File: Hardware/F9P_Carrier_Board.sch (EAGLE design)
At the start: 82 parts, among them J4 U.FL, J5 QWIIC_RIGHT_ANGLE, J6 MICROMOD-2222-C, J8 JTAG, U1 U-BLOX_ZED-F9P, U5 AP7361C-33

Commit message: Updates nets on the 100k at VREG, adds descpription of SPI jumper, adds VBAT testpoint
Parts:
- added TP3: TEST-POINT3X5, SparkFun-Connectors:TEST-POINT3X5
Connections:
- net V_BATT: now also TP3.1
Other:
- note added: "Close this jumper to enable SPI."
- moved on the sheet: BYP, C1, C13, C2, C5, C6, C7, D1, F2, MEAS, R5, U5

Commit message: Renames the erroneously named SCL/CLK net to SCLK/SCK
* Reroutes so that SCL and SCK are connected
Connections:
- removed net SCL/CLK: J10.7, J5.4, J6.SPI_SCK, R12A.2
- net SCL/SCK: now also J10.7, J5.4, J6.SPI_SCK, R12A.2
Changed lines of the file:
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@@
 <pinref part="J6" gate="J1" pin="I2C_SCL"/>
+</segment>
+<segment>
+<wire x1="106.68" y1="193.04" x2="109.22" y2="193.04" width="0.1524" layer="91"/>
+<label x="109.22" y="193.04" size="1.27" layer="95" xref="yes"/>
+<pinref part="J6" gate="J1" pin="SPI_SCK"/>
+</segment>
+<segment>
+<pinref part="J5" gate="G$1" pin="4"/>
+<wire x1="276.86" y1="63.5" x2="271.78" y2="63.5" width="0.1524" layer="91"/>
+<label x="276.86" y="63.5" size="1.27" layer="95" xref="yes"/>
+</segment>
+<segment>
+<wire x1="302.26" y1="50.8" x2="314.96" y2="50.8" width="0.1524" layer="91"/>
+<label x="314.96" y="50.8" size="1.27" layer="95" font="vector" xref="yes"/>
+<pinref part="J10" gate="G$1" pin="7"/>
+</segment>
+<segment>
+<wire x1="365.76" y1="170.18" x2="368.3" y2="170.18" width="0.1524" layer="91"/>
+<label x="368.3" y="170.18" size="1.27" layer="95" xref="yes"/>
+<pinref part="R12" gate="A" pin="2"/>
 </segment>
 </net>
@@
 </segment>
 </net>
-<net name="SCL/CLK" class="0">
-<segment>
-<pinref part="J5" gate="G$1" pin="4"/>
-<wire x1="276.86" y1="63.5" x2="271.78" y2="63.5" width="0.1524" layer="91"/>
-<label x="276.86" y="63.5" size="1.27" layer="95" xref="yes"/>
-</segment>
-<segment>
-<wire x1="106.68" y1="193.04" x2="109.22" y2="193.04" width="0.1524" layer="91"/>
-<label x="109.22" y="193.04" size="1.27" layer="95" xref="yes"/>
-<pinref part="J6" gate="J1" pin="SPI_SCK"/>
-</segment>
-<segment>
-<wire x1="302.26" y1="50.8" x2="314.96" y2="50.8" width="0.1524" layer="91"/>
-<label x="314.96" y="50.8" size="1.27" layer="95" font="vector" xref="yes"/>
-<pinref part="J10" gate="G$1" pin="7"/>
-</segment>
-<segment>
-<wire x1="365.76" y1="170.18" x2="368.3" y2="170.18" width="0.1524" layer="91"/>
-<label x="368.3" y="170.18" size="1.27" layer="95" xref="yes"/>
-<pinref part="R12" gate="A" pin="2"/>
-</segment>
-</net>

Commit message: Rolls version to v10, moves some vias, deletes I2C_INT net (not used)
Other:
- note added: "v10"
- note removed: "v01"
- moved on the sheet: C8, E1, FB1, J4, J9, R17

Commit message: Adjusts battery placement on board so that it's mostly out of the way
* Breaks out a few general purpose pins to a 6 pin header at the bottom of the board
* Adds text to led and enable jumpers
* Adds text about interrupt
* Adds connection from interrupt on ublox module to micromod connector.
* Fixes "processor" silk
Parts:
- added J7: (no value), SparkFun-Connectors:CONN_06NO_SILK_NO_POP
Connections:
- removed net I2C_!INT: J6.I2C_!INT!
- new net A0: J6.A0, J7.2
- new net A1: J6.A1, J7.3
- new net D1: J6.D1/CAM_TRIG, J7.4
- new net G0/D2: J6.G0/BUS0, J7.5
- net GND: now also J7.1, J7.6
- net INT: now also J6.I2C_!INT!
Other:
- note added: "Close "EN" jumper to allow processor control over 3.3V power."
- note added: "Cut jumpers to remove respective LEDs"
- note added: "Interrupt is not enabled by default. Check ublox datasheet for more information."
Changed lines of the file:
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@@
 <part name="TP3" library="SparkFun-Connectors" deviceset="TEST-POINT" device="3X5"/>
 <part name="SUPPLY15" library="SparkFun-PowerSymbols" deviceset="V_BATT" device=""/>
+<part name="J7" library="SparkFun-Connectors" deviceset="CONN_06" device="NO_SILK_NO_POP"/>
+<part name="GND26" library="SparkFun-PowerSymbols" deviceset="GND" device=""/>
 </parts>
 <sheets>
@@
 <text x="388.62" y="165.1" size="1.778" layer="97" font="vector">Close this jumper
 to enable SPI.</text>
+<text x="53.34" y="60.96" size="1.778" layer="97" font="vector">Cut jumpers to remove respective LEDs</text>
+<text x="5.08" y="208.28" size="1.778" layer="97" font="vector">Close "EN" jumper to allow processor
+control over 3.3V power.</text>
+<text x="370.84" y="187.96" size="1.778" layer="97" font="vector">Interrupt is not enabled by default.
+Check ublox datasheet for more information.</text>
+<wire x1="393.7" y1="185.42" x2="393.7" y2="175.26" width="0.1524" layer="97" style="dashdot"/>
+<wire x1="393.7" y1="175.26" x2="375.92" y2="175.26" width="0.1524" layer="97" style="dashdot"/>
 </plain>
 <instances>
@@
 <instance part="SUPPLY15" gate="G$1" x="195.58" y="10.16" smashed="yes">
 <attribute name="VALUE" x="195.58" y="12.954" size="1.778" layer="96" align="bottom-center"/>
+</instance>
+<instance part="J7" gate="G$1" x="264.16" y="17.78" smashed="yes">
+<attribute name="VALUE" x="259.08" y="7.874" size="1.778" layer="96" font="vector"/>
+<attribute name="NAME" x="259.08" y="28.448" size="1.778" layer="95" font="vector"/>
+</instance>
+<instance part="GND26" gate="1" x="271.78" y="7.62" smashed="yes">
+<attribute name="VALUE" x="271.78" y="7.366" size="1.778" layer="96" align="top-center"/>
 </instance>
 </instances>
@@
 <pinref part="GND7" gate="1" pin="GND"/>
 <wire x1="210.82" y1="195.58" x2="210.82" y2="185.42" width="0.1524" layer="91"/>
+</segment>
+<segment>
+<pinref part="J7" gate="G$1" pin="6"/>
+<wire x1="269.24" y1="25.4" x2="271.78" y2="25.4" width="0.1524" layer="91"/>
+<wire x1="271.78" y1="25.4" x2="271.78" y2="12.7" width="0.1524" layer="91"/>
+<pinref part="J7" gate="G$1" pin="1"/>
+<wire x1="271.78" y1="12.7" x2="271.78" y2="10.16" width="0.1524" layer="91"/>
+<wire x1="269.24" y1="12.7" x2="271.78" y2="12.7" width="0.1524" layer="91"/>
+<junction x="271.78" y="12.7"/>
+<pinref part="GND26" gate="1" pin="GND"/>
 </segment>
 </net>
@@
 </segment>
 </net>
-<net name="I2C_!INT" class="0">
-<segment>
-<wire x1="60.96" y1="139.7" x2="58.42" y2="139.7" width="0.1524" layer="91"/>
-<pinref part="J6" gate="J1" pin="I2C_!INT!"/>
-</segment>
-</net>
 <net name="N$5" class="0">
 <segment>
@@
 <label x="368.3" y="175.26" size="1.27" layer="95" xref="yes"/>
 <pinref part="R11" gate="A" pin="2"/>
+</segment>
+<segment>
+<pinref part="J6" gate="J1" pin="I2C_!INT!"/>
+<wire x1="60.96" y1="139.7" x2="58.42" y2="139.7" width="0.1524" layer="91"/>
+<label x="58.42" y="139.7" size="1.27" layer="95" rot="R180" xref="yes"/>
 </segment>
 </net>
@@
 </segment>
 </net>
+<net name="D1" class="0">
+<segment>
+<pinref part="J6" gate="J1" pin="D1/CAM_TRIG"/>
+<wire x1="106.68" y1="167.64" x2="109.22" y2="167.64" width="0.1524" layer="91"/>
+<label x="109.22" y="167.64" size="1.27" layer="95" xref="yes"/>
+</segment>
+<segment>
+<pinref part="J7" gate="G$1" pin="4"/>
+<wire x1="269.24" y1="20.32" x2="274.32" y2="20.32" width="0.1524" layer="91"/>
+<label x="274.32" y="20.32" size="1.27" layer="95" xref="yes"/>
+</segment>
+</net>
+<net name="G0/D2" class="0">
+<segment>
+<pinref part="J6" gate="J1" pin="G0/BUS0"/>
+<wire x1="106.68" y1="144.78" x2="109.22" y2="144.78" width="0.1524" layer="91"/>
+<label x="109.22" y="144.78" size="1.27" layer="95" xref="yes"/>
+</segment>
+<segment>
+<pinref part="J7" gate="G$1" pin="5"/>
+<wire x1="269.24" y1="22.86" x2="274.32" y2="22.86" width="0.1524" layer="91"/>
+<label x="274.32" y="22.86" size="1.27" layer="95" xref="yes"/>
+</segment>
+</net>
+<net name="A1" class="0">
+<segment>
+<pinref part="J6" gate="J1" pin="A1"/>
+<wire x1="106.68" y1="177.8" x2="109.22" y2="177.8" width="0.1524" layer="91"/>
+<label x="109.22" y="177.8" size="1.27" layer="95" xref="yes"/>
+</segment>
+<segment>
+<pinref part="J7" gate="G$1" pin="3"/>
+<wire x1="269.24" y1="17.78" x2="274.32" y2="17.78" width="0.1524" layer="91"/>
+<label x="274.32" y="17.78" size="1.27" layer="95" xref="yes"/>
+</segment>
+</net>
+<net name="A0" class="0">
+<segment>
+<pinref part="J6" gate="J1" pin="A0"/>
+<wire x1="106.68" y1="180.34" x2="109.22" y2="180.34" width="0.1524" layer="91"/>
+<label x="109.22" y="180.34" size="1.27" layer="95" xref="yes"/>
+</segment>
+<segment>
+<pinref part="J7" gate="G$1" pin="2"/>
+<wire x1="269.24" y1="15.24" x2="274.32" y2="15.24" width="0.1524" layer="91"/>
+<label x="274.32" y="15.24" size="1.27" layer="95" xref="yes"/>
+</segment>
+</net>

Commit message: Adds I2C address to schematic, swaps SMA connector to female version
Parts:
- J4: device SparkFun-RF:ANTENNA-SMA-GROUNDEDEDGE_RPSMA_SMD -> SparkFun-RF:ANTENNA-SMA-GROUNDEDEDGE_SMA_SMD
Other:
- note added: "I2C unshifted 7 bit address: 0x42"
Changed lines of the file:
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@@
 <part name="R16" library="SparkFun-Resistors" deviceset="27OHM" device=""/>
 <part name="D4" library="SparkFun-IC-Power" deviceset="PRTR5V0U2" device="F"/>
-<part name="J4" library="SparkFun-RF" deviceset="ANTENNA-SMA-GROUNDED" device="EDGE_RPSMA_SMD" value="U.FL"/>
+<part name="J4" library="SparkFun-RF" deviceset="ANTENNA-SMA-GROUNDED" device="EDGE_SMA_SMD" value="U.FL"/>
 <part name="GND14" library="SparkFun-PowerSymbols" deviceset="GND" device=""/>
 <part name="GND17" library="SparkFun-PowerSymbols" deviceset="GND" device=""/>
@@
 <wire x1="393.7" y1="185.42" x2="393.7" y2="175.26" width="0.1524" layer="97" style="dashdot"/>
 <wire x1="393.7" y1="175.26" x2="375.92" y2="175.26" width="0.1524" layer="97" style="dashdot"/>
+<text x="312.42" y="116.84" size="1.778" layer="97" font="vector">I2C unshifted 7 bit address: 0x42</text>
 </plain>
 <instances>

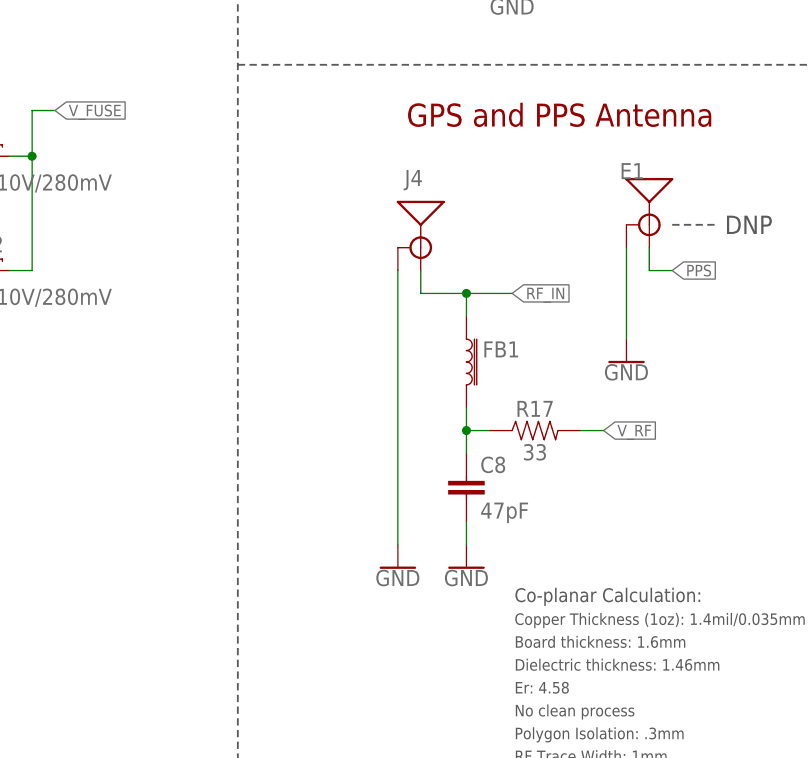
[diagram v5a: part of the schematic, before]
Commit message: Adds diode protection to antenna
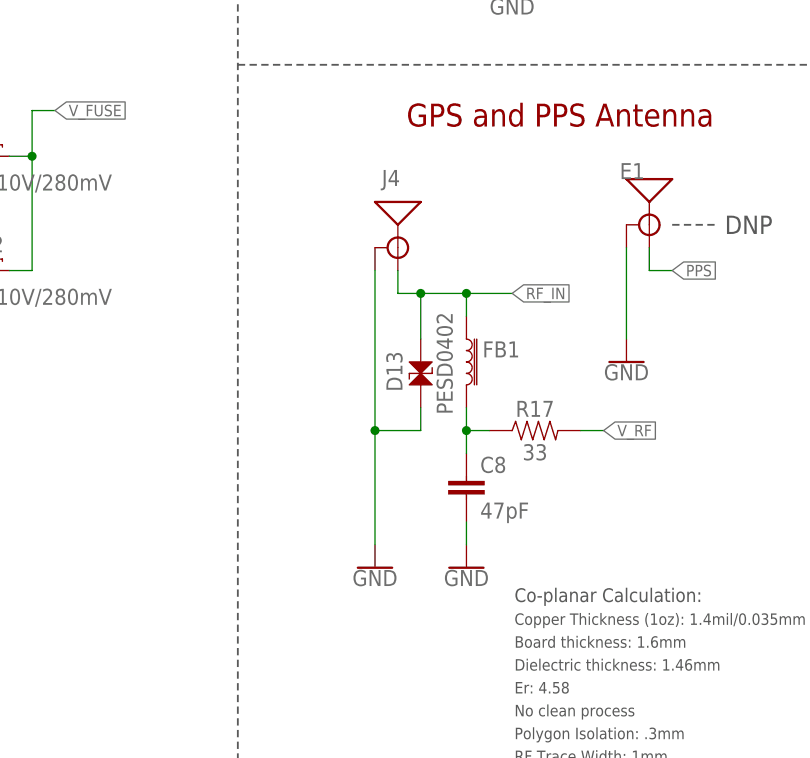
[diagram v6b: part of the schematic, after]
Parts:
- added D13: PESD0402, SparkFun-DiscreteSemi:PESD0402
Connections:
- net GND: now also D13.1
- net RF_IN: now also D13.2
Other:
- moved on the sheet: J4
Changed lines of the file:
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@@
 <layer number="56" name="wert" color="7" fill="1" visible="no" active="no"/>
 <layer number="57" name="tCAD" color="7" fill="1" visible="no" active="no"/>
+<layer number="58" name="bCAD" color="7" fill="1" visible="no" active="no"/>
 <layer number="59" name="tCarbon" color="7" fill="1" visible="no" active="no"/>
 <layer number="60" name="bCarbon" color="7" fill="1" visible="no" active="no"/>
@@
 <layer number="250" name="Descript" color="3" fill="1" visible="no" active="no"/>
 <layer number="251" name="SMDround" color="12" fill="11" visible="no" active="no"/>
+<layer number="253" name="Extra" color="7" fill="1" visible="no" active="no"/>
 <layer number="254" name="cooling" color="7" fill="1" visible="no" active="no"/>
 <layer number="255" name="routoute" color="7" fill="1" visible="no" active="no"/>
@@
 <part name="J7" library="SparkFun-Connectors" deviceset="CONN_06" device="NO_SILK_NO_POP"/>
 <part name="GND26" library="SparkFun-PowerSymbols" deviceset="GND" device=""/>
+<part name="D13" library="SparkFun-DiscreteSemi" deviceset="PESD0402" device=""/>
 </parts>
 <sheets>
@@
 <attribute name="VALUE" x="342.9" y="243.586" size="1.778" layer="96" align="top-left"/>
 </instance>
-<instance part="J4" gate="G$1" x="187.96" y="195.58" smashed="yes" rot="MR0">
-<attribute name="NAME" x="188.214" y="202.438" size="1.778" layer="95" rot="MR0"/>
-</instance>
-<instance part="GND14" gate="1" x="185.42" y="160.02" smashed="yes" rot="MR0">
-<attribute name="VALUE" x="185.42" y="159.766" size="1.778" layer="96" rot="MR0" align="top-center"/>
+<instance part="J4" gate="G$1" x="185.42" y="195.58" smashed="yes" rot="MR0">
+<attribute name="NAME" x="185.674" y="202.438" size="1.778" layer="95" rot="MR0"/>
+</instance>
+<instance part="GND14" gate="1" x="182.88" y="160.02" smashed="yes" rot="MR0">
+<attribute name="VALUE" x="182.88" y="159.766" size="1.778" layer="96" rot="MR0" align="top-center"/>
 </instance>
 <instance part="GND17" gate="1" x="193.04" y="160.02" smashed="yes">
@@
 <instance part="GND26" gate="1" x="271.78" y="7.62" smashed="yes">
 <attribute name="VALUE" x="271.78" y="7.366" size="1.778" layer="96" align="top-center"/>
+</instance>
+<instance part="D13" gate="G$1" x="187.96" y="180.34" smashed="yes" rot="R90">
+<attribute name="NAME" x="185.928" y="179.578" size="1.778" layer="95" font="vector" rot="R90"/>
+<attribute name="VALUE" x="189.738" y="177.038" size="1.778" layer="96" font="vector" rot="R90" align="top-left"/>
 </instance>
 </instances>
@@
 <pinref part="J4" gate="G$1" pin="GND"/>
 <pinref part="GND14" gate="1" pin="GND"/>
-<wire x1="185.42" y1="193.04" x2="185.42" y2="162.56" width="0.1524" layer="91"/>
+<wire x1="182.88" y1="193.04" x2="182.88" y2="175.26" width="0.1524" layer="91"/>
+<pinref part="D13" gate="G$1" pin="1"/>
+<wire x1="182.88" y1="175.26" x2="182.88" y2="162.56" width="0.1524" layer="91"/>
+<wire x1="187.96" y1="177.8" x2="187.96" y2="175.26" width="0.1524" layer="91"/>
+<wire x1="187.96" y1="175.26" x2="182.88" y2="175.26" width="0.1524" layer="91"/>
+<junction x="182.88" y="175.26"/>
 </segment>
 <segment>
@@
 <pinref part="J4" gate="G$1" pin="SIGNAL"/>
 <wire x1="193.04" y1="190.5" x2="187.96" y2="190.5" width="0.1524" layer="91"/>
-<wire x1="187.96" y1="190.5" x2="187.96" y2="193.04" width="0.1524" layer="91"/>
+<wire x1="187.96" y1="190.5" x2="185.42" y2="190.5" width="0.1524" layer="91"/>
+<wire x1="185.42" y1="190.5" x2="185.42" y2="193.04" width="0.1524" layer="91"/>
 <junction x="193.04" y="190.5"/>
 <pinref part="FB1" gate="G$1" pin="1"/>
-</segment>
-<segment>
+<pinref part="D13" gate="G$1" pin="2"/>
+<wire x1="187.96" y1="185.42" x2="187.96" y2="190.5" width="0.1524" layer="91"/>
+<junction x="187.96" y="190.5"/>
+</segment>
+<segment>

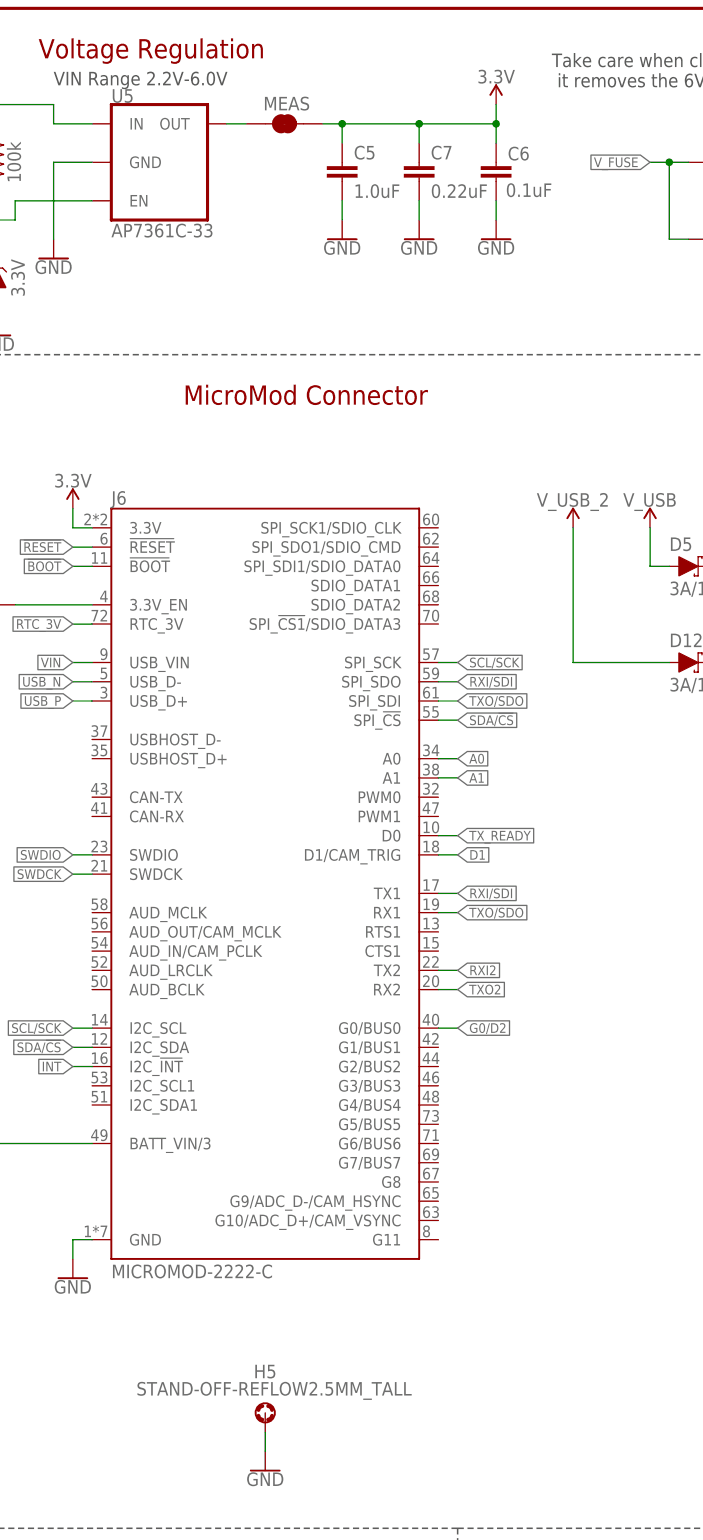
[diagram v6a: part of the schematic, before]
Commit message: Updates silk, moves 1x6 header to the left .005"
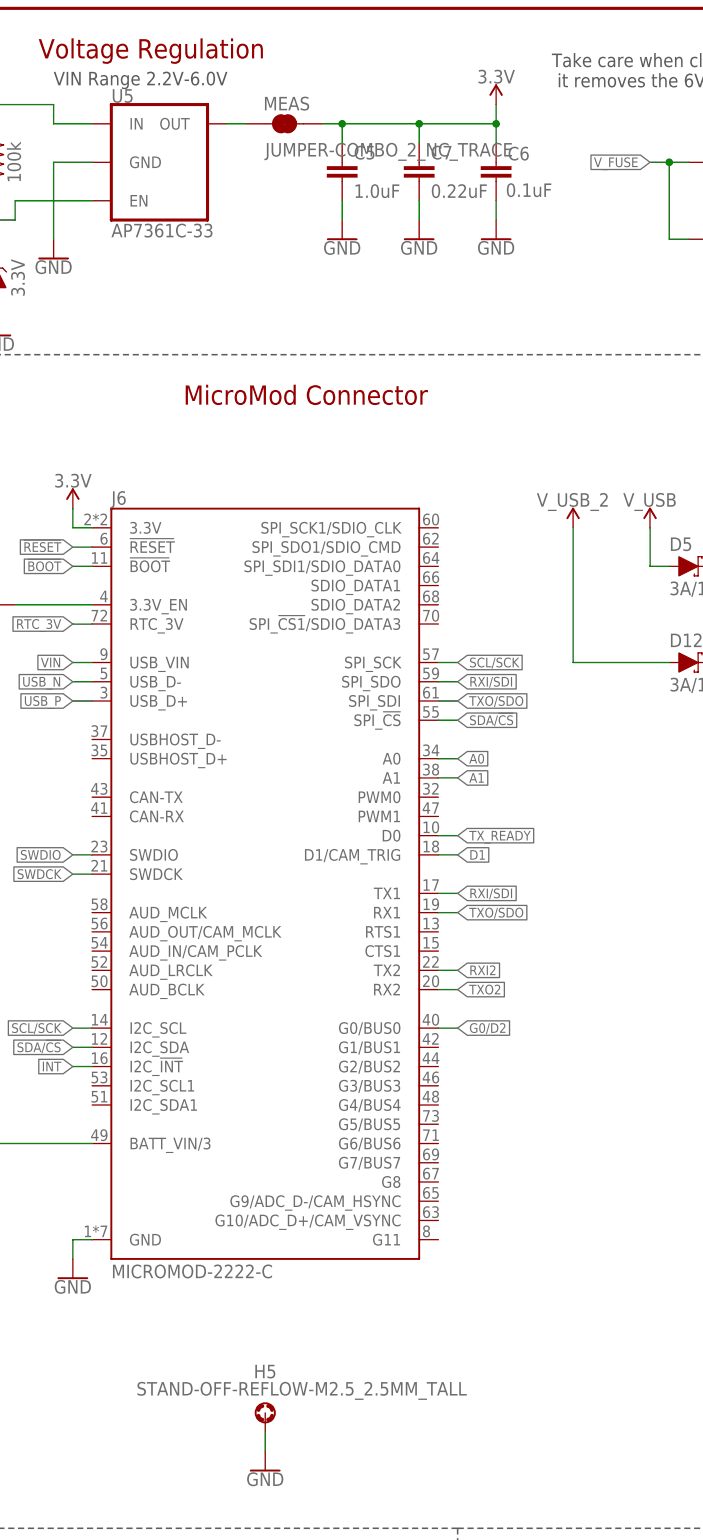
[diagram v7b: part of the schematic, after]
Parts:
- H5: value STAND-OFF-REFLOW2.5MM_TALL -> STAND-OFF-REFLOW-M2.5_2.5MM_TALL; device SparkFun-Hardware:STAND-OFF-REFLOW2.5MM_TALL -> SparkFun-Hardware:STAND-OFF-REFLOW-M2.5_2.5MM_TALL

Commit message: Replaces SMD SMA connector with PTH one
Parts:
- J4: device SparkFun-RF:ANTENNA-SMA-GROUNDEDEDGE_SMA_SMD -> SparkFun-RF:ANTENNA-SMA-GROUNDEDEDGE_SMA
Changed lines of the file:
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@@
 <part name="R16" library="SparkFun-Resistors" deviceset="27OHM" device=""/>
 <part name="D4" library="SparkFun-IC-Power" deviceset="PRTR5V0U2" device="F"/>
-<part name="J4" library="SparkFun-RF" deviceset="ANTENNA-SMA-GROUNDED" device="EDGE_SMA_SMD" value="U.FL"/>
+<part name="J4" library="SparkFun-RF" deviceset="ANTENNA-SMA-GROUNDED" device="EDGE_SMA" value="U.FL"/>
 <part name="GND14" library="SparkFun-PowerSymbols" deviceset="GND" device=""/>
 <part name="GND17" library="SparkFun-PowerSymbols" deviceset="GND" device=""/>
